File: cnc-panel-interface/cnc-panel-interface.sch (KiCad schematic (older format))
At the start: 42 parts, among them J1 BusIn, J10 Mounting hole, J11 Mounting hole, J2 BusOut, J3 Out1, J4 Out2, J5 Rows1, J6 Rows2, J7 Com, J8 Mounting hole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

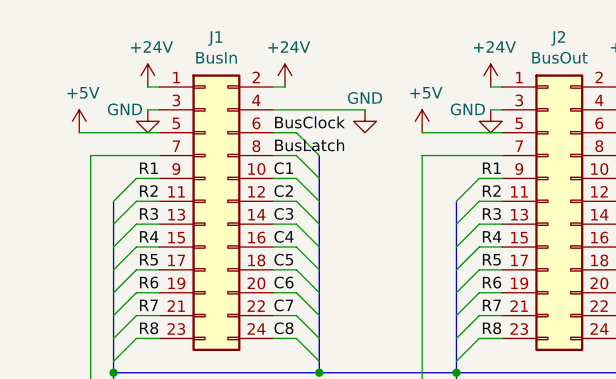
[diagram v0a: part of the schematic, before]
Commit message: Add power flags
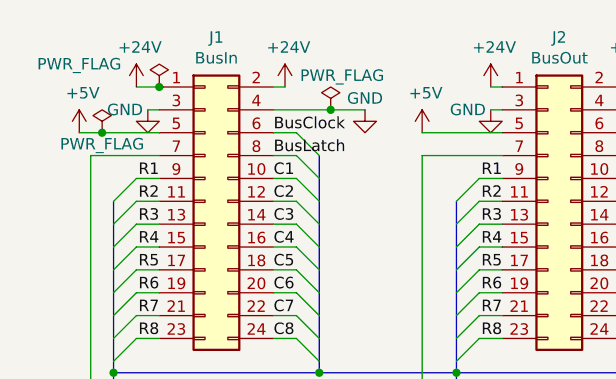
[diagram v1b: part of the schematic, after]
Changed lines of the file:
@@
 L power:+24V #PWR0107
 U 1 1 5F8C90C2
-P 1450 850
-F 0 "#PWR0107" H 1450 700 50  0001 C CNN
-F 1 "+24V" H 1465 1023 50  0000 C CNN
-F 2 "" H 1450 850 50  0001 C CNN
-F 3 "" H 1450 850 50  0001 C CNN
-	1    1450 850
-	1    0    0    -1
-$EndComp
-Wire Wire Line
-	1500 850  1450 850
+P 1400 850
+F 0 "#PWR0107" H 1400 700 50  0001 C CNN
+F 1 "+24V" H 1415 1023 50  0000 C CNN
+F 2 "" H 1400 850 50  0001 C CNN
+F 3 "" H 1400 850 50  0001 C CNN
+	1    1400 850
+	1    0    0    -1
+$EndComp
+Wire Wire Line
+	1500 850  1400 850
 $Comp
 L power:+5V #PWR0108
@@
 $EndComp
 Wire Wire Line
-	1500 1050 1150 1050
-Wire Wire Line
-	2000 950  2400 950
+	1500 1050 1250 1050
+Wire Wire Line
+	2000 950  2250 950
 Text Label 2000 1050 0    50   ~ 0
 BusClock
@@
 Wire Wire Line
 	4850 2600 5250 2600
+$Comp
+L power:PWR_FLAG #FLG0101
+U 1 1 5F717479
+P 1500 850
+F 0 "#FLG0101" H 1500 925 50  0001 C CNN
+F 1 "PWR_FLAG" H 1150 950 50  0000 C CNN
+F 2 "" H 1500 850 50  0001 C CNN
+F 3 "~" H 1500 850 50  0001 C CNN
+	1    1500 850
+	1    0    0    -1
+$EndComp
+Connection ~ 1500 850
+$Comp
+L power:PWR_FLAG #FLG0102
+U 1 1 5F718535
+P 2250 950
+F 0 "#FLG0102" H 2250 1025 50  0001 C CNN
+F 1 "PWR_FLAG" H 2300 1100 50  0000 C CNN
+F 2 "" H 2250 950 50  0001 C CNN
+F 3 "~" H 2250 950 50  0001 C CNN
+	1    2250 950
+	1    0    0    -1
+$EndComp
+Connection ~ 2250 950
+Wire Wire Line
+	2250 950  2400 950
+$Comp
+L power:PWR_FLAG #FLG0103
+U 1 1 5F718998
+P 1250 1050
+F 0 "#FLG0103" H 1250 1125 50  0001 C CNN
+F 1 "PWR_FLAG" H 1250 1000 50  0000 C CNN
+F 2 "" H 1250 1050 50  0001 C CNN
+F 3 "~" H 1250 1050 50  0001 C CNN
+	1    1250 1050
+	1    0    0    -1
+$EndComp
+Connection ~ 1250 1050
+Wire Wire Line
+	1250 1050 1150 1050
 Wire Bus Line
 	1300 2100 1300 4400
